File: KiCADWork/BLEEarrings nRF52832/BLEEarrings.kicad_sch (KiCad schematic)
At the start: 11 parts, among them J4 Conn_01x06_Pin, SW1 TK-6580B-1, U1 AP7343D-33W5-7

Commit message: Small Bits
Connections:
- net at C4.1, SW1.3, TP1.1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: now also U1.1 (VIN)
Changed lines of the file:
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@@
     (stroke (width 0) (type default))
   )
-  (wire (pts (xy 117.475 121.92) (xy 125.095 121.92))
+  (wire (pts (xy 114.935 121.92) (xy 125.095 121.92))
     (stroke (width 0) (type default))
   )
@@
     (stroke (width 0) (type default))
   )
-  (wire (pts (xy 139.065 56.515) (xy 132.715 56.515))
+  (wire (pts (xy 132.715 56.515) (xy 139.7 56.515))
     (stroke (width 0) (type default))
   )
@@
     (stroke (width 0) (type default))
   )
-  (wire (pts (xy 116.84 117.475) (xy 125.095 117.475))
+  (wire (pts (xy 119.38 117.475) (xy 125.095 117.475))
     (stroke (width 0) (type default))
   )
@@
     (stroke (width 0) (type default))
   )
-  (wire (pts (xy 117.475 125.095) (xy 125.095 125.095))
+  (wire (pts (xy 115.57 125.095) (xy 125.095 125.095))
     (stroke (width 0) (type default))
   )
@@
     (effects (font (size 1 1)) (justify left bottom))
   )
-  (global_label "Tx" (shape input) (at 117.475 121.92 180) (fields_autoplaced)
-    (effects (font (size 1.27 1.27)) (justify right))
-    (property "Intersheetrefs" "${INTERSHEET_REFS}" (at 112.4941 121.92 0)
+  (global_label "Tx" (shape input) (at 114.935 121.92 180) (fields_autoplaced)
+    (effects (font (size 1.27 1.27)) (justify right))
+    (property "Intersheetrefs" "${INTERSHEET_REFS}" (at 109.9541 121.92 0)
       (effects (font (size 1.27 1.27)) (justify right) hide)
     )
@@
     )
   )
-  (global_label "Rx" (shape input) (at 117.475 125.095 180) (fields_autoplaced)
-    (effects (font (size 1.27 1.27)) (justify right))
-    (property "Intersheetrefs" "${INTERSHEET_REFS}" (at 112.1917 125.095 0)
+  (global_label "Rx" (shape input) (at 115.57 125.095 180) (fields_autoplaced)
+    (effects (font (size 1.27 1.27)) (justify right))
+    (property "Intersheetrefs" "${INTERSHEET_REFS}" (at 110.2867 125.095 0)
       (effects (font (size 1.27 1.27)) (justify right) hide)
     )
@@
     )
   )
-  (global_label "nRESET" (shape input) (at 116.84 117.475 180) (fields_autoplaced)
-    (effects (font (size 1.27 1.27)) (justify right))
-    (property "Intersheetrefs" "${INTERSHEET_REFS}" (at 106.9607 117.475 0)
-      (effects (font (size 1.27 1.27)) (justify right) hide)
-    )
+  (global_label "nRESET" (shape input) (at 119.38 117.475 180) (fields_autoplaced)
+    (effects (font (size 1.27 1.27)) (justify right))
+    (property "Intersheetrefs" "${INTERSHEET_REFS}" (at 109.5007 117.475 0)
+      (effects (font (size 1.27 1.27)) (justify right) hide)
+    )

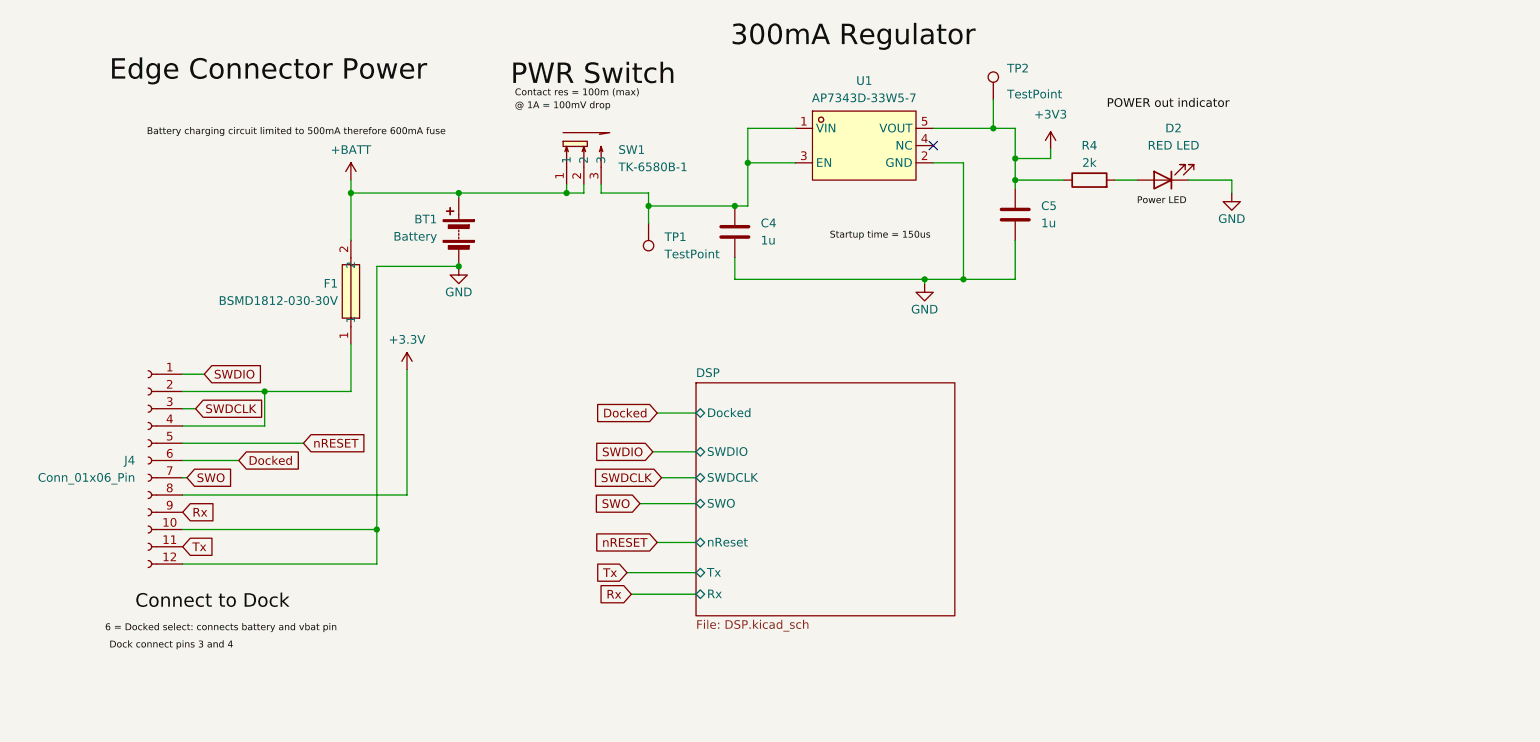
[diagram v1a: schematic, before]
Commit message: New Chip NRF52833
large changes
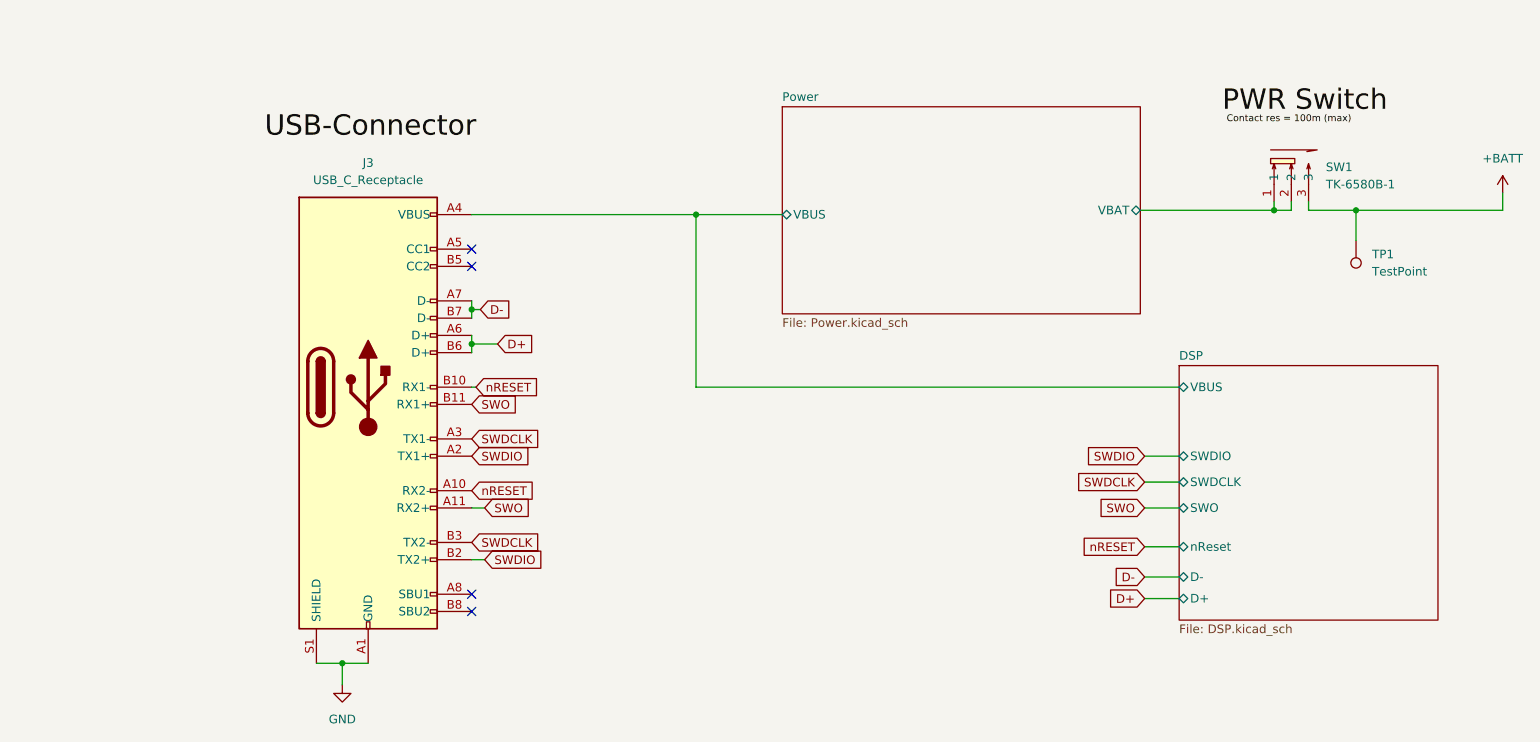
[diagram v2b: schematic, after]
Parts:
- removed BT1: Battery, easyeda2kicad:CONN-TH_1.25-2AW, symbol Device:Battery
- removed C4, C5: 1u, Capacitor_SMD:C_0402_1005Metric_Pad0.74x0.62mm_HandSolder, symbol Device:C
- removed D2: RED LED, LED_SMD:LED_0603_1608Metric_Pad1.05x0.95mm_HandSolder, symbol Device:LED
- removed F1: BSMD1812-030-30V, easyeda2kicad:F1812, symbol easyeda2kicad:BSMD1812-030-30V
- removed J4: Conn_01x06_Pin, easyeda2kicad:HDR-SMD_PM127VS-12-12-H34-4.5-R, symbol Connector:Conn_01x12_Socket
- removed R4: 2k, Resistor_SMD:R_0402_1005Metric_Pad0.72x0.64mm_HandSolder, symbol Device:R
- removed TP2: TestPoint, TestPoint:TestPoint_Pad_D1.0mm, symbol Connector:TestPoint
- removed U1: AP7343D-33W5-7, easyeda2kicad:SOT-23-5_L2.9-W1.6-P0.95-LS2.8-BR, symbol easyeda2kicad:AP7343D-33W5-7
- added J3: USB_C_Receptacle, easyeda2kicad:TYPE-C-SMD_C9900025773, symbol Connector:USB_C_Receptacle
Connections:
- net +BATT: now also SW1.3, TP1.1; no longer SW1.1, SW1.2
- net GND: now also J3.A1 (GND), J3.A12 (GND), J3.B1 (GND), J3.B12 (GND), J3.S1 (SHIELD)
- net SWDCLK: now also J3.A3 (TX1-), J3.B3 (TX2-)
- net SWDIO: now also J3.A2 (TX1+), J3.B2 (TX2+)
- net SWO: now also J3.A11 (RX2+), J3.B11 (RX1+)
- net nRESET: now also J3.A10 (RX2-), J3.B10 (RX1-)
- new net D+: J3.A6 (D+), J3.B6 (D+)
- new net D-: J3.A7 (D-), J3.B7 (D-)
- new net DSP/VBUS: J3.A4 (VBUS), J3.A9 (VBUS), J3.B4 (VBUS), J3.B9 (VBUS)
- new net Power/VBAT: SW1.1, SW1.2
- no-connect marks 1 -> 4
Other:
- added sheet Power (Power.kicad_sch)
- sheet DSP ports: added D+, D-, VBUS; removed Docked, Rx, Tx
- moved on the sheet: SW1, TP1

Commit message: Dock Updates
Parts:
- added D2: USBLC6-2SC6_C2687116, easyeda2kicad:SOT-23-6_L2.9-W1.6-P0.95-LS2.8-BL, symbol easyeda2kicad:USBLC6-2SC6_C2687116
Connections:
- net D+: now also D2.4 (I/O2); no longer J3.A6 (D+), J3.B6 (D+)
- net D-: now also D2.6 (I/O1); no longer J3.A7 (D-), J3.B7 (D-)
- net DSP/VBUS: now also D2.5 (VBUS)
- net GND: now also J3.A5 (CC1), J3.B5 (CC2), D2.2 (GND)
- new net: D2.1 (I/O1), J3.A7 (D-), J3.B7 (D-)
- new net: D2.3 (I/O2), J3.A6 (D+), J3.B6 (D+)
- no-connect marks 4 -> 2
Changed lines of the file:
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@@
   (junction (at 92.075 88.265) (diameter 0) (color 0 0 0 0)
   )
+  (junction (at 109.22 76.835) (diameter 0) (color 0 0 0 0)
+  )
+  (junction (at 133.985 92.075) (diameter 0) (color 0 0 0 0)
+  )
   (junction (at 92.075 83.185) (diameter 0) (color 0 0 0 0)
   )
@@
   )
   (junction (at 210.185 68.58) (diameter 0) (color 0 0 0 0)
+  )
+  (junction (at 123.19 69.215) (diameter 0) (color 0 0 0 0)
   )
   (no_connect (at 92.075 127.635))
   (no_connect (at 92.075 125.095))
-  (no_connect (at 92.075 76.835))
-  (no_connect (at 92.075 74.295))
   (wire (pts (xy 191.135 112.395) (xy 196.215 112.395))
     (stroke (width 0) (type default))
   )
+  (wire (pts (xy 92.075 74.295) (xy 109.22 74.295))
+    (stroke (width 0) (type default))
+  )
+  (wire (pts (xy 109.22 74.295) (xy 109.22 76.835))
+    (stroke (width 0) (type default))
+  )
   (wire (pts (xy 222.25 68.58) (xy 243.84 68.58))
     (stroke (width 0) (type default))
@@
     (stroke (width 0) (type default))
   )
+  (wire (pts (xy 121.285 83.185) (xy 125.095 83.185))
+    (stroke (width 0) (type default))
+  )
   (wire (pts (xy 93.98 102.235) (xy 92.075 102.235))
     (stroke (width 0) (type default))
   )
+  (wire (pts (xy 121.285 88.265) (xy 122.555 88.265))
+    (stroke (width 0) (type default))
+  )
   (wire (pts (xy 93.98 117.475) (xy 92.075 117.475))
     (stroke (width 0) (type default))
   )
+  (wire (pts (xy 97.79 85.725) (xy 97.79 92.075))
+    (stroke (width 0) (type default))
+  )
   (wire (pts (xy 222.25 68.58) (xy 222.25 73.025))
     (stroke (width 0) (type default))
@@
     (stroke (width 0) (type default))
   )
+  (wire (pts (xy 133.985 92.075) (xy 133.985 101.6))
+    (stroke (width 0) (type default))
+  )
   (wire (pts (xy 73.025 135.255) (xy 76.835 135.255))
     (stroke (width 0) (type default))
@@
     (stroke (width 0) (type default))
   )
+  (wire (pts (xy 133.985 92.075) (xy 133.985 76.835))
+    (stroke (width 0) (type default))
+  )
   (wire (pts (xy 135.89 69.215) (xy 144.145 69.215))
     (stroke (width 0) (type default))
@@
     (stroke (width 0) (type default))
   )
-  (wire (pts (xy 92.075 88.265) (xy 112.395 88.265))
+  (wire (pts (xy 92.075 88.265) (xy 98.425 88.265))
+    (stroke (width 0) (type default))
+  )
+  (wire (pts (xy 123.19 69.215) (xy 123.19 85.725))
     (stroke (width 0) (type default))
   )
@@
     (stroke (width 0) (type default))
   )
-  (wire (pts (xy 92.075 69.215) (xy 135.89 69.215))
+  (wire (pts (xy 92.075 69.215) (xy 123.19 69.215))
     (stroke (width 0) (type default))
   )
@@
     (stroke (width 0) (type default))
   )
+  (wire (pts (xy 92.075 76.835) (xy 109.22 76.835))
+    (stroke (width 0) (type default))
+  )
+  (wire (pts (xy 123.19 69.215) (xy 135.89 69.215))
+    (stroke (width 0) (type default))
+  )
   (wire (pts (xy 92.075 81.915) (xy 92.075 83.185))
     (stroke (width 0) (type default))
@@
     (stroke (width 0) (type default))
   )
+  (wire (pts (xy 98.425 85.725) (xy 97.79 85.725))
+    (stroke (width 0) (type default))
+  )
   (wire (pts (xy 191.135 125.73) (xy 196.215 125.73))
     (stroke (width 0) (type default))
@@
   )
   (wire (pts (xy 73.025 138.43) (xy 73.025 135.255))
+    (stroke (width 0) (type default))
+  )
+  (wire (pts (xy 109.22 76.835) (xy 133.985 76.835))
+    (stroke (width 0) (type default))
+  )
+  (wire (pts (xy 97.79 92.075) (xy 133.985 92.075))
+    (stroke (width 0) (type default))
+  )
+  (wire (pts (xy 121.285 85.725) (xy 123.19 85.725))
     (stroke (width 0) (type default))
   )
@@
     (effects (font (size 1 1)) (justify left bottom))
   )
+  (label "Can be charged individually" (at 60.325 59.69 0) (fields_autoplaced)
+    (effects (font (size 1 1)) (justify left bottom))
+  )
   (label "PWR Switch" (at 202.565 54.61 0) (fields_autoplaced)
     (effects (font (size 3 3)) (justify left bottom))
   )
-  (label "USB-Connector" (at 61.595 58.42 0) (fields_autoplaced)
+  (label "USB-Connector" (at 60.325 57.15 0) (fields_autoplaced)
     (effects (font (size 3 3)) (justify left bottom))
   )
+  (label "No resistors = 500mA limit with individual charge" (at 94.615 65.405 0) (fields_autoplaced)
+    (effects (font (size 1 1)) (justify left bottom))
+  )
+  (label "power output managed otherwise by dock" (at 94.615 67.945 0) (fields_autoplaced)
+    (effects (font (size 1 1)) (justify left bottom))
+  )
   (global_label "D-" (shape input) (at 191.135 122.555 180) (fields_autoplaced)
     (effects (font (size 1.27 1.27)) (justify right))
@@
     )
   )
-  (global_label "D+" (shape input) (at 112.395 88.265 0) (fields_autoplaced)
-    (effects (font (size 1.27 1.27)) (justify left))
-    (property "Intersheetrefs" "${INTERSHEET_REFS}" (at 118.2226 88.265 0)
+  (global_label "D+" (shape input) (at 122.555 88.265 0) (fields_autoplaced)
+    (effects (font (size 1.27 1.27)) (justify left))
+    (property "Intersheetrefs" "${INTERSHEET_REFS}" (at 128.3826 88.265 0)
       (effects (font (size 1.27 1.27)) (justify left) hide)
     )
@@
     )
   )
-  (global_label "D-" (shape input) (at 98.425 83.185 0) (fields_autoplaced)
-    (effects (font (size 1.27 1.27)) (justify left))
-    (property "Intersheetrefs" "${INTERSHEET_REFS}" (at 104.2526 83.185 0)
+  (global_label "D-" (shape input) (at 125.095 83.185 0) (fields_autoplaced)
+    (effects (font (size 1.27 1.27)) (justify left))
+    (property "Intersheetrefs" "${INTERSHEET_REFS}" (at 130.9226 83.185 0)
       (effects (font (size 1.27 1.27)) (justify left) hide)
     )
@@
         (path "/fde3e4b3-cb63-4f5f-903c-f7733537b674"
           (reference "SW1") (unit 1)
+        )
+      )
+    )
+  )
+  (symbol (lib_id "easyeda2kicad:USBLC6-2SC6_C2687116") (at 109.855 85.725 0) (unit 1)
+    (in_bom yes) (on_board yes) (dnp no) (fields_autoplaced)
+    (property "Reference" "D2" (at 109.855 76.2 0)
+      (effects (font (size 1.27 1.27)))
+    )
+    (property "Value" "USBLC6-2SC6_C2687116" (at 109.855 78.74 0)
+      (effects (font (size 1.27 1.27)))
+    )
+    (property "Footprint" "easyeda2kicad:SOT-23-6_L2.9-W1.6-P0.95-LS2.8-BL" (at 109.855 95.885 0)
+      (effects (font (size 1.27 1.27)) hide)
+    )
+    (property "Datasheet" "" (at 109.855 85.725 0)
+      (effects (font (size 1.27 1.27)) hide)
+    )
+    (property "LCSC Part" "C2687116" (at 109.855 98.425 0)
+      (effects (font (size 1.27 1.27)) hide)
+    )
+    (pin "6")
+    (pin "3")
+    (pin "4")
+    (pin "2")
+    (pin "1")
+    (pin "5")
+    (instances
+      (project "BLEEarrings"
+        (path "/fde3e4b3-cb63-4f5f-903c-f7733537b674"
+          (reference "D2") (unit 1)
         )
       )
@@
         )
       )
+    )
+  )
+  (symbol (lib_id "power:GND") (at 133.985 101.6 0) (unit 1)
+    (in_bom yes) (on_board yes) (dnp no) (fields_autoplaced)
+    (property "Reference" "#PWR023" (at 133.985 107.95 0)
+      (effects (font (size 1.27 1.27)) hide)
+    )
+    (property "Value" "GND" (at 133.985 106.045 0)
+      (effects (font (size 1.27 1.27)))
+    )
+    (property "Footprint" "" (at 133.985 101.6 0)
+      (effects (font (size 1.27 1.27)) hide)
+    )
+    (property "Datasheet" "" (at 133.985 101.6 0)
+      (effects (font (size 1.27 1.27)) hide)
+    )
+    (pin "1")
+    (instances
+      (project "BLEEarrings"
+        (path "/fde3e4b3-cb63-4f5f-903c-f7733537b674"
+          (reference "#PWR023") (unit 1)
+        )
+      )

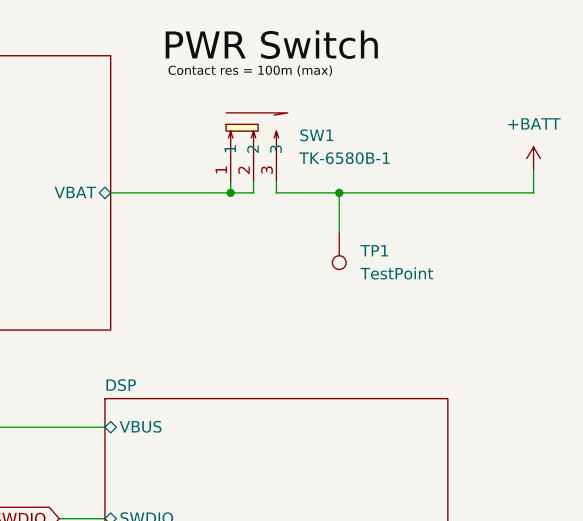
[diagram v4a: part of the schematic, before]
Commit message: Routing Started on Earrings Again
- Only small routing changes made
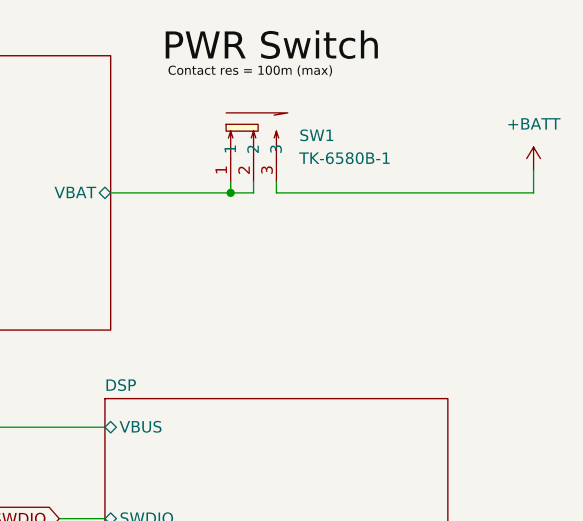
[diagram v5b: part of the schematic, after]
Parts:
- removed TP1: TestPoint, TestPoint:TestPoint_Pad_D1.0mm, symbol Connector:TestPoint
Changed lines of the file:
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@@
   (junction (at 135.89 69.215) (diameter 0) (color 0 0 0 0)
-  )
-  (junction (at 222.25 68.58) (diameter 0) (color 0 0 0 0)
   )
   (junction (at 210.185 68.58) (diameter 0) (color 0 0 0 0)
@@
     (stroke (width 0) (type default))
   )
-  (wire (pts (xy 222.25 68.58) (xy 243.84 68.58))
-    (stroke (width 0) (type default))
-  )
   (wire (pts (xy 93.98 104.775) (xy 92.075 104.775))
     (stroke (width 0) (type default))
@@
     (stroke (width 0) (type default))
   )
-  (wire (pts (xy 222.25 68.58) (xy 222.25 73.025))
-    (stroke (width 0) (type default))
-  )
   (wire (pts (xy 191.135 122.555) (xy 196.215 122.555))
     (stroke (width 0) (type default))
@@
     (stroke (width 0) (type default))
   )
-  (wire (pts (xy 215.265 68.58) (xy 222.25 68.58))
+  (wire (pts (xy 215.265 68.58) (xy 243.84 68.58))
     (stroke (width 0) (type default))
   )
@@
         (path "/fde3e4b3-cb63-4f5f-903c-f7733537b674"
           (reference "#PWR02") (unit 1)
-        )
-      )
-    )
-  )
-  (symbol (lib_id "Connector:TestPoint") (at 222.25 73.025 180) (unit 1)
-    (in_bom yes) (on_board yes) (dnp no) (fields_autoplaced)
-    (property "Reference" "TP1" (at 224.6122 75.057 0)
-      (effects (font (size 1.27 1.27)) (justify right))
-    )
-    (property "Value" "TestPoint" (at 224.6122 77.597 0)
-      (effects (font (size 1.27 1.27)) (justify right))
-    )
-    (property "Footprint" "TestPoint:TestPoint_Pad_D1.0mm" (at 217.17 73.025 0)
-      (effects (font (size 1.27 1.27)) hide)
-    )
-    (property "Datasheet" "~" (at 217.17 73.025 0)
-      (effects (font (size 1.27 1.27)) hide)
-    )
-    (pin "1")
-    (instances
-      (project "Dock"
-        (path "/6f84fb5e-0715-49fa-a507-16643db39fa4/fa45a25b-726e-4689-8d43-3622783c5f9d"
-          (reference "TP1") (unit 1)
-        )
-      )
-      (project "BLEEarrings"
-        (path "/fde3e4b3-cb63-4f5f-903c-f7733537b674"
-          (reference "TP3") (unit 1)
         )
       )
@@
           (reference "#PWR01") (unit 1)
         )
-        (path "/fde3e4b3-cb63-4f5f-903c-f7733537b674/37cadbd7-6b4e-4ad6-85fe-82f50abfc793"
-          (reference "#PWR022") (unit 1)
-        )
-      )
+      )

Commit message: Ignoring Backups
More Dock progress
All local backups removed
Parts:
- J3: LCSC Part (none) -> C5156605
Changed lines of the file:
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@@
+      (effects (font (size 1.27 1.27)) hide)
+    )
+    (property "LCSC Part" "C5156605 " (at 76.835 94.615 0)
       (effects (font (size 1.27 1.27)) hide)
     )

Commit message: Beautiful Skilkscreen Added
Dock schematic intial draft complete
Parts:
- added R1 (x2): 5k1, Resistor_SMD:R_0402_1005Metric_Pad0.72x0.64mm_HandSolder, symbol Device:R
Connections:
- net GND: now also R1.1, R1.1; no longer J3.A5 (CC1), J3.B5 (CC2)
- net SWDCLK renamed SWDCLK_L
- net SWDIO renamed SWDIO_L
- net SWO renamed SWO_L
- net nRESET renamed DSP/nReset
- new net: J3.A5 (CC1), R1.2
- new net: J3.B5 (CC2), R1.2
